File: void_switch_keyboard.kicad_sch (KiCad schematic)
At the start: 166 parts, among them J1 QWIIC, U1 CD74HC4067SM, U10 GH39FKSW, U11 GH39FKSW, U12 GH39FKSW, U13 GH39FKSW, U14 GH39FKSW, U15 GH39FKSW, U16 GH39FKSW, U17 GH39FKSW, U18 GH39FKSW, U19 GH39FKSW, U2 CD74HC4067SM, U20 GH39FKSW, U21 GH39FKSW, U22 GH39FKSW, U23 GH39FKSW, U24 GH39FKSW, U25 GH39FKSW, U26 GH39FKSW, U27 GH39FKSW, U28 GH39FKSW, U29 GH39FKSW, U3 CD74HC4067SM, U30 GH39FKSW, U31 GH39FKSW, U32 GH39FKSW, U33 GH39FKSW, U34 GH39FKSW, U35 GH39FKSW, U36 GH39FKSW, U37 GH39FKSW, U38 GH39FKSW, U39 GH39FKSW, U4 CD74HC4067SM, U40 GH39FKSW, U41 GH39FKSW, U42 GH39FKSW, U43 GH39FKSW, U44 GH39FKSW, U45 GH39FKSW, U46 GH39FKSW, U47 GH39FKSW, U48 GH39FKSW, U49 GH39FKSW, U5 CD74HC4067SM, U50 GH39FKSW, U51 GH39FKSW, U52 GH39FKSW, U53 GH39FKSW, U54 GH39FKSW, U55 GH39FKSW, U56 GH39FKSW, U57 GH39FKSW, U58 GH39FKSW, U59 GH39FKSW, U6 BlackPill_STLINK, U60 GH39FKSW, U61 GH39FKSW, U62 GH39FKSW, U63 GH39FKSW, U64 GH39FKSW, U65 GH39FKSW, U66 GH39FKSW, U67 GH39FKSW, U68 GH39FKSW, U69 GH39FKSW, U7 GH39FKSW, U70 GH39FKSW, U71 GH39FKSW, U72 GH39FKSW, U73 GH39FKSW, U74 GH39FKSW, U75 GH39FKSW, U76 GH39FKSW, U8 GH39FKSW, U9 GH39FKSW

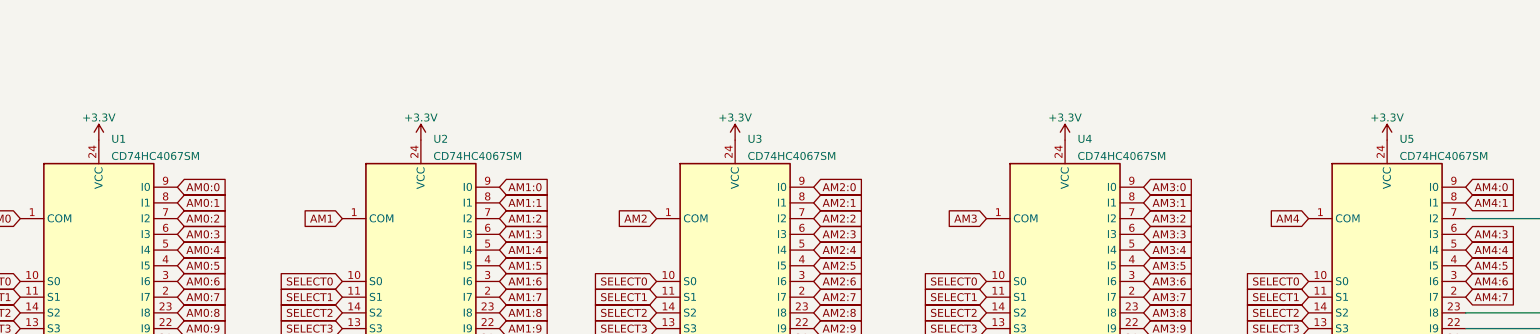
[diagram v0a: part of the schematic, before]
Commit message: Updated silkscreen and fixed the analog multiplexer references so they're AM0-AM4 instead of U1-U5.
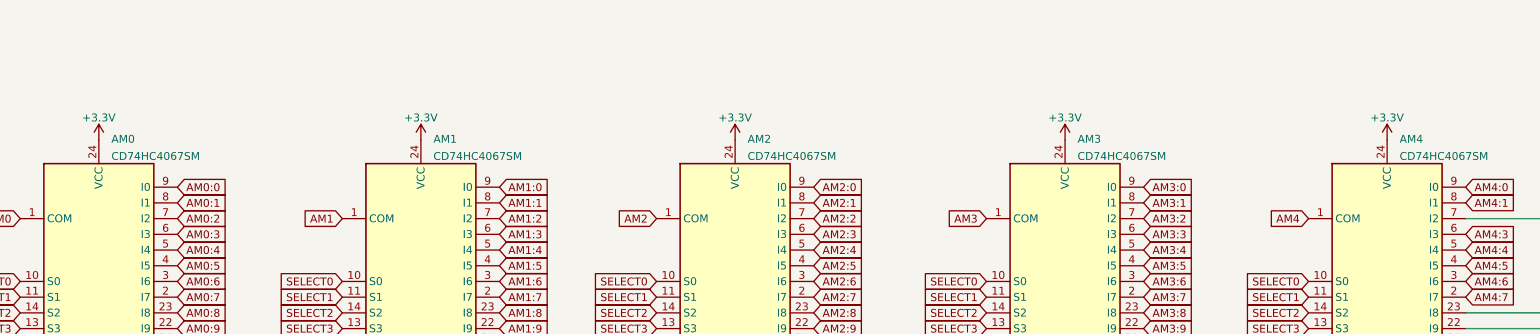
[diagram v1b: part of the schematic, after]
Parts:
- renumbered U1 to AM0, U2 to AM1, U3 to AM2, U4 to AM3, U5 to AM4
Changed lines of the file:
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@@
   (symbol (lib_id "74xx:CD74HC4067SM") (at 229.235 64.135 0) (unit 1)
     (in_bom yes) (on_board yes) (fields_autoplaced)
-    (property "Reference" "U2" (id 0) (at 231.2544 38.5785 0)
+    (property "Reference" "AM1" (id 0) (at 231.2544 38.5785 0)
       (effects (font (size 1.27 1.27)) (justify left))
     )
@@
   (symbol (lib_id "74xx:CD74HC4067SM") (at 385.445 64.135 0) (unit 1)
     (in_bom yes) (on_board yes) (fields_autoplaced)
-    (property "Reference" "U5" (id 0) (at 387.4644 38.5785 0)
+    (property "Reference" "AM4" (id 0) (at 387.4644 38.5785 0)
       (effects (font (size 1.27 1.27)) (justify left))
     )
@@
   (symbol (lib_id "74xx:CD74HC4067SM") (at 280.035 64.135 0) (unit 1)
     (in_bom yes) (on_board yes) (fields_autoplaced)
-    (property "Reference" "U3" (id 0) (at 282.0544 38.5785 0)
+    (property "Reference" "AM2" (id 0) (at 282.0544 38.5785 0)
       (effects (font (size 1.27 1.27)) (justify left))
     )
@@
   (symbol (lib_id "74xx:CD74HC4067SM") (at 177.165 64.135 0) (unit 1)
     (in_bom yes) (on_board yes) (fields_autoplaced)
-    (property "Reference" "U1" (id 0) (at 179.1844 38.5785 0)
+    (property "Reference" "AM0" (id 0) (at 179.1844 38.5785 0)
       (effects (font (size 1.27 1.27)) (justify left))
     )
@@
   (symbol (lib_id "74xx:CD74HC4067SM") (at 333.375 64.135 0) (unit 1)
     (in_bom yes) (on_board yes) (fields_autoplaced)
-    (property "Reference" "U4" (id 0) (at 335.3944 38.5785 0)
+    (property "Reference" "AM3" (id 0) (at 335.3944 38.5785 0)
       (effects (font (size 1.27 1.27)) (justify left))
     )
@@
       (reference "#PWR0164") (unit 1) (value "GND") (footprint "")
     )
+    (path "/9c8d9ee2-2b97-4096-9f63-e88b1d368336"
+      (reference "AM0") (unit 1) (value "CD74HC4067SM") (footprint "Package_SO:SSOP-24_5.3x8.2mm_P0.65mm")
+    )
     (path "/0ec16a1d-0028-4415-9ec9-609629941555"
       (reference "AM0:0") (unit 1) (value "Super") (footprint "void_switch:VoidSwitch_1u_SMD")
@@
       (reference "AM0:15") (unit 1) (value "LAlt") (footprint "void_switch:VoidSwitch_1u_SMD")
     )
+    (path "/5c474c49-8034-4016-ae16-323a11cc68b9"
+      (reference "AM1") (unit 1) (value "CD74HC4067SM") (footprint "Package_SO:SSOP-24_5.3x8.2mm_P0.65mm")
+    )
     (path "/b14843e9-f206-4e81-8ccc-e9e6032caacb"
       (reference "AM1:0") (unit 1) (value "F") (footprint "void_switch:VoidSwitch_1u_SMD")
@@
       (reference "AM1:15") (unit 1) (value "V") (footprint "void_switch:VoidSwitch_1u_SMD")
     )
+    (path "/90cf972e-cbcc-40c8-b79e-37debddbfe69"
+      (reference "AM2") (unit 1) (value "CD74HC4067SM") (footprint "Package_SO:SSOP-24_5.3x8.2mm_P0.65mm")
+    )
     (path "/99be7986-f41e-4c29-8fdf-ab70a7107aba"
       (reference "AM2:2") (unit 1) (value "M") (footprint "void_switch:VoidSwitch_1u_SMD")
@@
       (reference "AM2:14") (unit 1) (value "More Fun") (footprint "void_switch:VoidSwitch_1u_SMD")
     )
+    (path "/db45c3c3-1250-48bc-a6ed-d093379eb4fb"
+      (reference "AM3") (unit 1) (value "CD74HC4067SM") (footprint "Package_SO:SSOP-24_5.3x8.2mm_P0.65mm")
+    )
     (path "/6b7bcce7-18cb-4aac-bf1b-037ea11d3c47"
       (reference "AM3:1") (unit 1) (value "Slash") (footprint "void_switch:VoidSwitch_1u_SMD")
@@
       (reference "AM3:14") (unit 1) (value "Menu") (footprint "void_switch:VoidSwitch_1u_SMD")
     )
+    (path "/8bc8bcc6-31ff-473a-8894-15a45eba39ad"
+      (reference "AM4") (unit 1) (value "CD74HC4067SM") (footprint "Package_SO:SSOP-24_5.3x8.2mm_P0.65mm")
+    )
     (path "/908d4b2c-9f05-4735-a5b7-7a3be944de69"
       (reference "AM4:0") (unit 1) (value "DOWN") (footprint "void_switch:VoidSwitch_1u_SMD")
@@
       (reference "R2") (unit 1) (value "2k2") (footprint "Resistor_SMD:R_0402_1005Metric")
     )
-    (path "/9c8d9ee2-2b97-4096-9f63-e88b1d368336"
-      (reference "U1") (unit 1) (value "CD74HC4067SM") (footprint "Package_SO:SSOP-24_5.3x8.2mm_P0.65mm")
-    )
-    (path "/5c474c49-8034-4016-ae16-323a11cc68b9"
-      (reference "U2") (unit 1) (value "CD74HC4067SM") (footprint "Package_SO:SSOP-24_5.3x8.2mm_P0.65mm")
-    )
-    (path "/90cf972e-cbcc-40c8-b79e-37debddbfe69"
-      (reference "U3") (unit 1) (value "CD74HC4067SM") (footprint "Package_SO:SSOP-24_5.3x8.2mm_P0.65mm")
-    )
-    (path "/db45c3c3-1250-48bc-a6ed-d093379eb4fb"
-      (reference "U4") (unit 1) (value "CD74HC4067SM") (footprint "Package_SO:SSOP-24_5.3x8.2mm_P0.65mm")
-    )
-    (path "/8bc8bcc6-31ff-473a-8894-15a45eba39ad"
-      (reference "U5") (unit 1) (value "CD74HC4067SM") (footprint "Package_SO:SSOP-24_5.3x8.2mm_P0.65mm")
-    )
     (path "/a22b0997-f941-4376-bbcf-55e3c72f43e0"

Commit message: Fixed the 1.25U keys having 1U footprints.
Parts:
- AM0:0, AM0:1, AM0:15, AM1:2, AM2:14, AM3:3: footprint void_switch:VoidSwitch_1u_SMD -> void_switch:VoidSwitch_1.25u_SMD
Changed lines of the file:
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@@
       (effects (font (size 0.9906 0.9906)))
     )
-    (property "Footprint" "void_switch:VoidSwitch_1u_SMD" (id 2) (at 133.985 217.805 0)
+    (property "Footprint" "void_switch:VoidSwitch_1.25u_SMD" (id 2) (at 133.985 217.805 0)
       (effects (font (size 1.27 1.27)) hide)
     )
@@
       (effects (font (size 0.9906 0.9906)))
     )
-    (property "Footprint" "void_switch:VoidSwitch_1u_SMD" (id 2) (at 103.505 217.805 0)
+    (property "Footprint" "void_switch:VoidSwitch_1.25u_SMD" (id 2) (at 103.505 217.805 0)
       (effects (font (size 1.27 1.27)) hide)
     )
@@
       (effects (font (size 0.9906 0.9906)))
     )
-    (property "Footprint" "void_switch:VoidSwitch_1u_SMD" (id 2) (at 309.88 217.805 0)
+    (property "Footprint" "void_switch:VoidSwitch_1.25u_SMD" (id 2) (at 309.88 217.805 0)
       (effects (font (size 1.27 1.27)) hide)
     )
@@
       (effects (font (size 0.9906 0.9906)))
     )
-    (property "Footprint" "void_switch:VoidSwitch_1u_SMD" (id 2) (at 193.675 217.805 0)
+    (property "Footprint" "void_switch:VoidSwitch_1.25u_SMD" (id 2) (at 193.675 217.805 0)
       (effects (font (size 1.27 1.27)) hide)
     )
@@
       (effects (font (size 0.9906 0.9906)))
     )
-    (property "Footprint" "void_switch:VoidSwitch_1u_SMD" (id 2) (at 340.995 217.805 0)
+    (property "Footprint" "void_switch:VoidSwitch_1.25u_SMD" (id 2) (at 340.995 217.805 0)
       (effects (font (size 1.27 1.27)) hide)
     )
@@
       (effects (font (size 0.9906 0.9906)))
     )
-    (property "Footprint" "void_switch:VoidSwitch_1u_SMD" (id 2) (at 163.83 217.805 0)
+    (property "Footprint" "void_switch:VoidSwitch_1.25u_SMD" (id 2) (at 163.83 217.805 0)
       (effects (font (size 1.27 1.27)) hide)
     )
@@
     )
     (path "/0ec16a1d-0028-4415-9ec9-609629941555"
-      (reference "AM0:0") (unit 1) (value "Super") (footprint "void_switch:VoidSwitch_1u_SMD")
+      (reference "AM0:0") (unit 1) (value "Super") (footprint "void_switch:VoidSwitch_1.25u_SMD")
     )
     (path "/848a481b-30b7-4332-a703-0dbdeacdda6b"
-      (reference "AM0:1") (unit 1) (value "LCtrl") (footprint "void_switch:VoidSwitch_1u_SMD")
+      (reference "AM0:1") (unit 1) (value "LCtrl") (footprint "void_switch:VoidSwitch_1.25u_SMD")
     )
     (path "/aeeaa5fb-6a99-4a18-89fb-9ec0d3bb4360"
@@
     )
     (path "/f7f4f904-fc49-41cd-ba42-70ee72eafb7c"
-      (reference "AM0:15") (unit 1) (value "LAlt") (footprint "void_switch:VoidSwitch_1u_SMD")
+      (reference "AM0:15") (unit 1) (value "LAlt") (footprint "void_switch:VoidSwitch_1.25u_SMD")
     )
     (path "/5c474c49-8034-4016-ae16-323a11cc68b9"
@@
     )
     (path "/ba3ebc1f-2c9b-4fe2-81cf-2056f41fd9b1"
-      (reference "AM1:2") (unit 1) (value "Fun") (footprint "void_switch:VoidSwitch_1u_SMD")
+      (reference "AM1:2") (unit 1) (value "Fun") (footprint "void_switch:VoidSwitch_1.25u_SMD")
     )
     (path "/a9eac101-8758-4335-8e16-8e921f96b408"
@@
     )
     (path "/b8d59f57-308a-4af8-a597-03a5aadeb752"
-      (reference "AM2:14") (unit 1) (value "More Fun") (footprint "void_switch:VoidSwitch_1u_SMD")
+      (reference "AM2:14") (unit 1) (value "More Fun") (footprint "void_switch:VoidSwitch_1.25u_SMD")
     )
     (path "/db45c3c3-1250-48bc-a6ed-d093379eb4fb"
@@
     )
     (path "/c7087234-c640-43bf-a58d-264ccbc622e3"
-      (reference "AM3:3") (unit 1) (value "RAlt") (footprint "void_switch:VoidSwitch_1u_SMD")
+      (reference "AM3:3") (unit 1) (value "RAlt") (footprint "void_switch:VoidSwitch_1.25u_SMD")
     )
     (path "/4b4105a6-2799-49c5-b57e-166b2eaa0870"

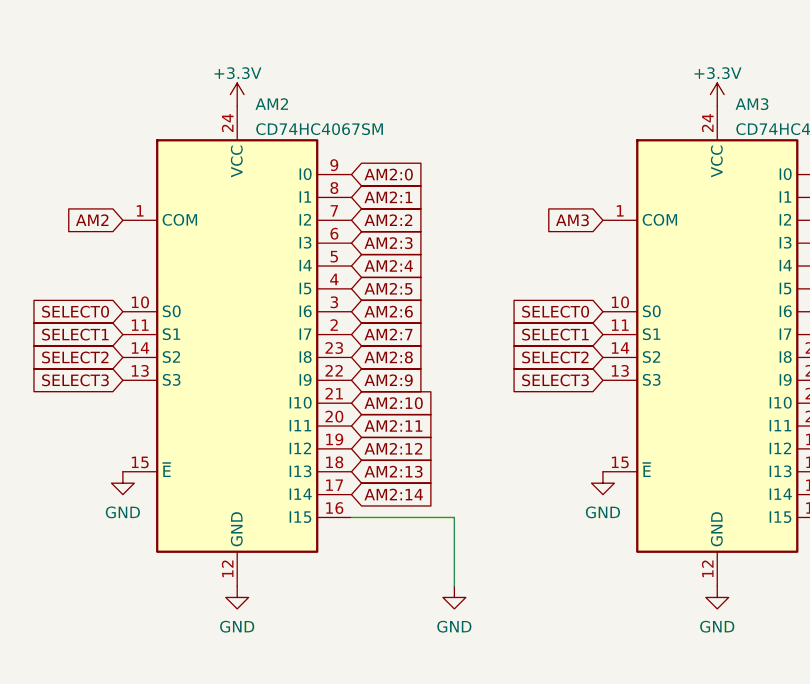
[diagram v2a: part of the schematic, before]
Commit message: Fixed AM0:0 and AM0:1 being left floating.  They're now connected to ground as they should be (because they're unused).
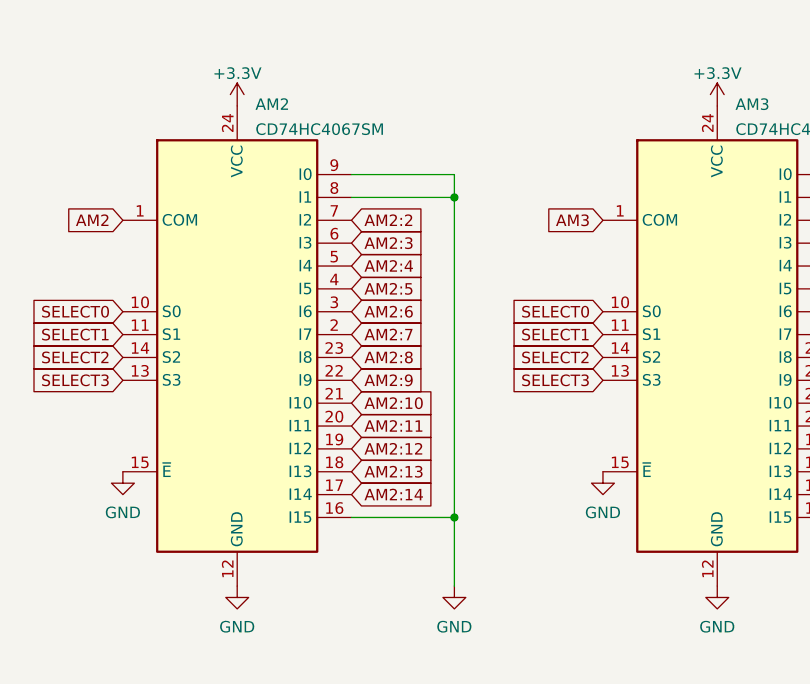
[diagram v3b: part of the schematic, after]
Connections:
- net AM2:0 is gone; now on net GND: AM2.9 (I0)
- net AM2:1 is gone; now on net GND: AM2.8 (I1)
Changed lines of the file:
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@@
   (junction (at 485.775 43.815) (diameter 0) (color 0 0 0 0)
   )
+  (junction (at 304.165 48.895) (diameter 0) (color 0 0 0 0)
+  )
   (junction (at 509.905 43.815) (diameter 0) (color 0 0 0 0)
   )
@@
   )
   (junction (at 411.48 74.295) (diameter 0) (color 0 0 0 0)
+  )
+  (junction (at 304.165 84.455) (diameter 0) (color 0 0 0 0)
   )
   (no_connect (at 65.405 51.435))
@@
     (stroke (width 0) (type default) (color 0 0 0 0))
   )
+  (wire (pts (xy 304.165 48.895) (xy 304.165 84.455))
+    (stroke (width 0) (type default) (color 0 0 0 0))
+  )
   (wire (pts (xy 509.905 52.705) (xy 498.475 52.705))
     (stroke (width 0) (type default) (color 0 0 0 0))
@@
     (stroke (width 0) (type default) (color 0 0 0 0))
   )
+  (wire (pts (xy 292.735 46.355) (xy 304.165 46.355))
+    (stroke (width 0) (type default) (color 0 0 0 0))
+  )
   (wire (pts (xy 104.14 26.67) (xy 104.14 29.21))
     (stroke (width 0) (type default) (color 0 0 0 0))
@@
     (stroke (width 0) (type default) (color 0 0 0 0))
   )
+  (wire (pts (xy 304.165 46.355) (xy 304.165 48.895))
+    (stroke (width 0) (type default) (color 0 0 0 0))
+  )
   (polyline (pts (xy 525.145 60.325) (xy 525.145 34.925))
     (stroke (width 0) (type default) (color 0 0 0 0))
@@
   )
   (wire (pts (xy 55.245 94.615) (xy 55.245 97.79))
+    (stroke (width 0) (type default) (color 0 0 0 0))
+  )
+  (wire (pts (xy 292.735 48.895) (xy 304.165 48.895))
     (stroke (width 0) (type default) (color 0 0 0 0))
   )
@@
     )
   )
-  (global_label "AM2:0" (shape input) (at 292.735 46.355 0) (fields_autoplaced)
-    (effects (font (size 1.27 1.27)) (justify left))
-    (property "Intersheet References" "${INTERSHEET_REFS}" (id 0) (at 300.7119 46.2756 0)
-      (effects (font (size 1.27 1.27)) (justify left) hide)
-    )
-  )
   (global_label "AM3:7" (shape input) (at 346.075 64.135 0) (fields_autoplaced)
     (effects (font (size 1.27 1.27)) (justify left))
@@
       (effects (font (size 1.27 1.27)) (justify left) hide)
     )
-  )
-  (global_label "AM2:1" (shape input) (at 292.735 48.895 0) (fields_autoplaced)
-    (effects (font (size 1.27 1.27)) (justify left))
-    (property "Intersheet References" "${INTERSHEET_REFS}" (id 0) (at 300.7119 48.8156 0)
-      (effects (font (size 1.27 1.27)) (justify left) hide)
-    )

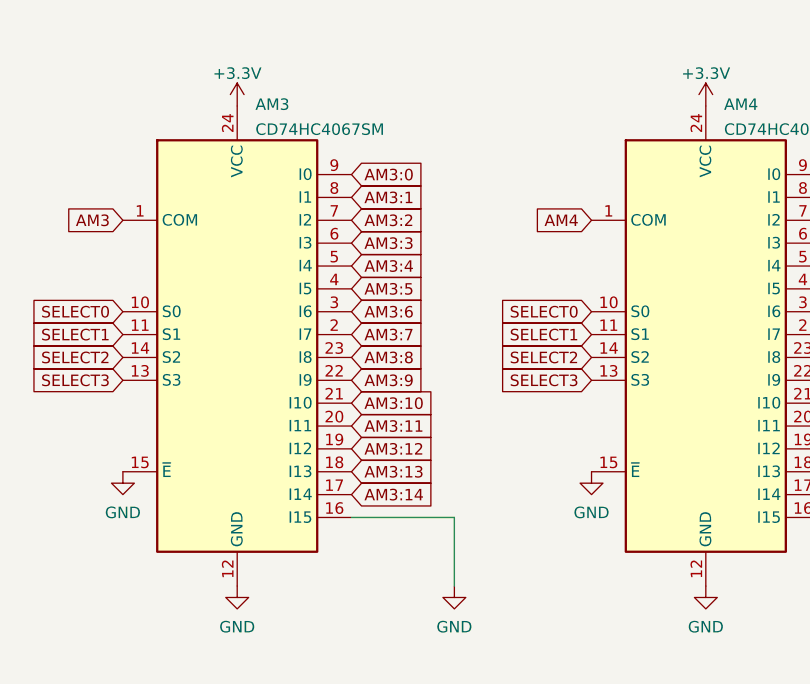
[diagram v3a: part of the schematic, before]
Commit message: Fixed a MUX pins that was left floating and added a bit of 3.3V and GND stitching to shorten the power/ground path here and there.
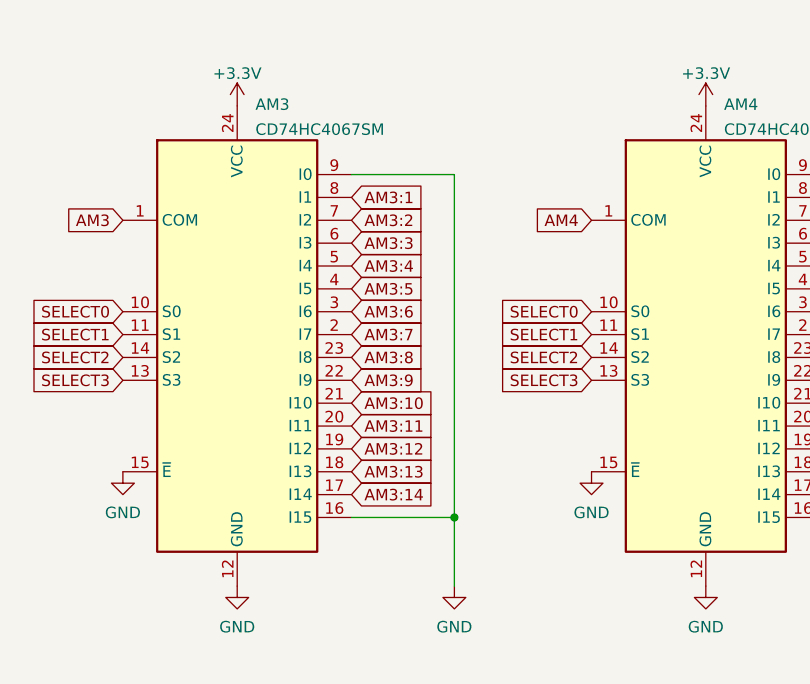
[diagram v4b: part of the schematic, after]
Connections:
- net AM3:0 is gone; now on net GND: AM3.9 (I0)
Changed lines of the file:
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@@
   (junction (at 411.48 66.675) (diameter 0) (color 0 0 0 0)
+  )
+  (junction (at 357.505 84.455) (diameter 0) (color 0 0 0 0)
   )
   (junction (at 411.48 74.295) (diameter 0) (color 0 0 0 0)
@@
     (stroke (width 0) (type default) (color 0 0 0 0))
   )
+  (wire (pts (xy 346.075 46.355) (xy 357.505 46.355))
+    (stroke (width 0) (type default) (color 0 0 0 0))
+  )
   (wire (pts (xy 50.165 97.79) (xy 52.705 97.79))
     (stroke (width 0) (type default) (color 0 0 0 0))
@@
   )
   (wire (pts (xy 292.735 46.355) (xy 304.165 46.355))
+    (stroke (width 0) (type default) (color 0 0 0 0))
+  )
+  (wire (pts (xy 357.505 46.355) (xy 357.505 84.455))
     (stroke (width 0) (type default) (color 0 0 0 0))
   )
@@
     )
   )
-  (global_label "AM3:0" (shape input) (at 346.075 46.355 0) (fields_autoplaced)
-    (effects (font (size 1.27 1.27)) (justify left))
-    (property "Intersheet References" "${INTERSHEET_REFS}" (id 0) (at 354.0519 46.2756 0)
-      (effects (font (size 1.27 1.27)) (justify left) hide)
-    )
-  )
